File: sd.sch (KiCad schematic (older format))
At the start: 8 parts, among them J5 Micro_SD_Card_Det, U14 IP4220CZ6, U15 IP4220CZ6

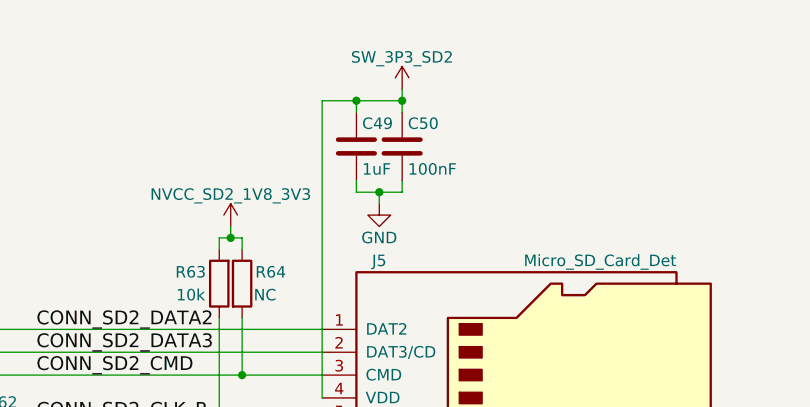
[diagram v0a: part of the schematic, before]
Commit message: Assign all associated signals to their respective pins on the EmCraft i.MX8M SoM
The ERC is now at the same state as the DART SoM schematic. Need to compare various aspects of the current schematic against the EmCraft reference design. The main buck-boost will likely need to be switched to a 5V regulator, or be configured to output 5V.

A regulator will likely need to be added which will output some VBAT voltage level (3.5~4.2V) for the M.2 cards. The SIM7100 for example requires at least 3.4V!
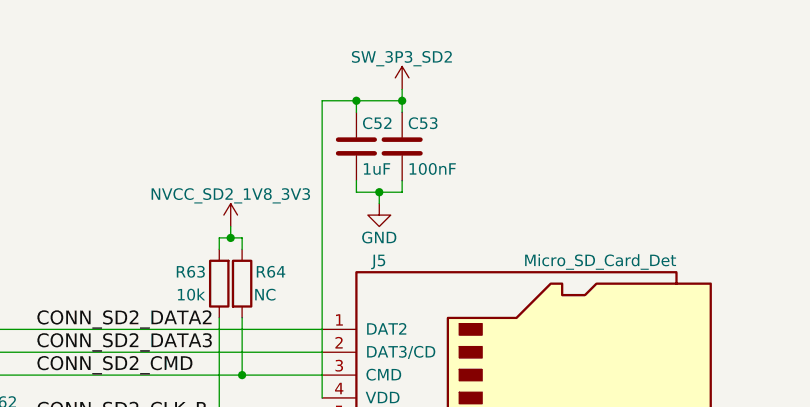
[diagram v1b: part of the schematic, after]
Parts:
- renumbered C49 to C52, C50 to C53
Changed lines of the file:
@@
 $EndComp
 $Comp
-L GND #PWR0119
+L GND #PWR0121
 U 1 1 5AC9FCAE
 P 5650 4550
-F 0 "#PWR0119" H 5650 4300 50  0001 C CNN
+F 0 "#PWR0121" H 5650 4300 50  0001 C CNN
 F 1 "GND" H 5650 4400 50  0000 C CNN
 F 2 "" H 5650 4550 50  0001 C CNN
@@
 $EndComp
 $Comp
-L GND #PWR0120
+L GND #PWR0122
 U 1 1 5ACA0128
 P 3850 4550
-F 0 "#PWR0120" H 3850 4300 50  0001 C CNN
+F 0 "#PWR0122" H 3850 4300 50  0001 C CNN
 F 1 "GND" H 3850 4400 50  0000 C CNN
 F 2 "" H 3850 4550 50  0001 C CNN
@@
 $EndComp
 $Comp
-L C C49
+L C C52
 U 1 1 5ACA0BD2
 P 4050 2800
-F 0 "C49" H 4075 2900 50  0000 L CNN
+F 0 "C52" H 4075 2900 50  0000 L CNN
 F 1 "1uF" H 4075 2700 50  0000 L CNN
 F 2 "" H 4088 2650 50  0001 C CNN
@@
 $EndComp
 $Comp
-L SW_3P3_SD2 #PWR0121
+L SW_3P3_SD2 #PWR0123
 U 1 1 5ACA0BF9
 P 4250 2550
-F 0 "#PWR0121" H 4250 2400 50  0001 C CNN
+F 0 "#PWR0123" H 4250 2400 50  0001 C CNN
 F 1 "SW_3P3_SD2" H 4250 2690 50  0000 C CNN
 F 2 "" H 4250 2550 50  0001 C CNN
@@
 $EndComp
 $Comp
-L NVCC_SD2_1V8_3V3 #PWR0122
+L NVCC_SD2_1V8_3V3 #PWR0124
 U 1 1 5ACA0C17
 P 3500 3150
-F 0 "#PWR0122" H 3500 3000 50  0001 C CNN
+F 0 "#PWR0124" H 3500 3000 50  0001 C CNN
 F 1 "NVCC_SD2_1V8_3V3" H 3500 3290 50  0000 C CNN
 F 2 "" H 3500 3150 50  0001 C CNN
@@
 $EndComp
 $Comp
-L C C50
+L C C53
 U 1 1 5ACA10D0
 P 4250 2800
-F 0 "C50" H 4275 2900 50  0000 L CNN
+F 0 "C53" H 4275 2900 50  0000 L CNN
 F 1 "100nF" H 4275 2700 50  0000 L CNN
 F 2 "" H 4288 2650 50  0001 C CNN
@@
 $EndComp
 $Comp
-L GND #PWR0123
+L GND #PWR0125
 U 1 1 5ACA12D0
 P 4150 3050
-F 0 "#PWR0123" H 4150 2800 50  0001 C CNN
+F 0 "#PWR0125" H 4150 2800 50  0001 C CNN
 F 1 "GND" H 4150 2900 50  0000 C CNN
 F 2 "" H 4150 3050 50  0001 C CNN
@@
 NoConn ~ 7200 3250
 $Comp
-L GND #PWR0124
+L GND #PWR0126
 U 1 1 5ACB9D67
 P 8400 4550
-F 0 "#PWR0124" H 8400 4300 50  0001 C CNN
+F 0 "#PWR0126" H 8400 4300 50  0001 C CNN
 F 1 "GND" H 8400 4400 50  0000 C CNN
 F 2 "" H 8400 4550 50  0001 C CNN
@@
 Connection ~ 8400 4200
 $Comp
-L NVCC_SD2_1V8_3V3 #PWR0125
+L NVCC_SD2_1V8_3V3 #PWR0127
 U 1 1 5ACB9F80
 P 7000 2550
-F 0 "#PWR0125" H 7000 2400 50  0001 C CNN
+F 0 "#PWR0127" H 7000 2400 50  0001 C CNN
 F 1 "NVCC_SD2_1V8_3V3" H 7000 2690 50  0000 C CNN
 F 2 "" H 7000 2550 50  0001 C CNN

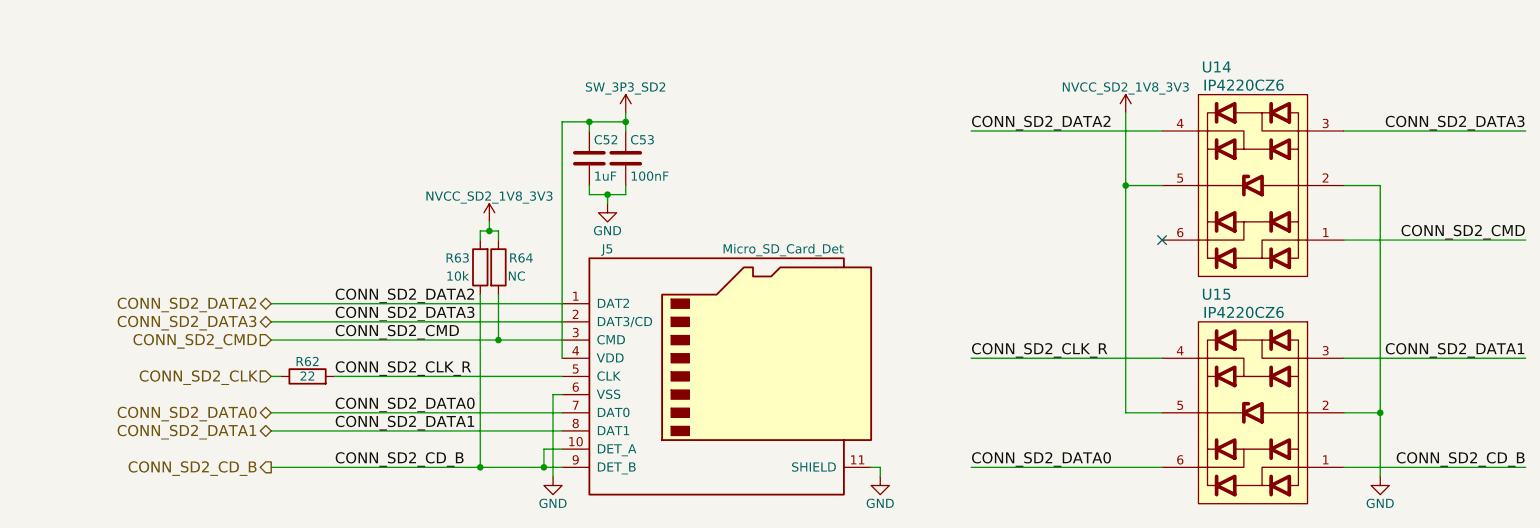
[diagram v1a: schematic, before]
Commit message: Use "Start to sheet number*100 and use first free number" designation, any new component added to the schematic will occupy the next available number in that sheet
For example: if sheet 2 has R201-R215 and we add a new resistor it will become R216.
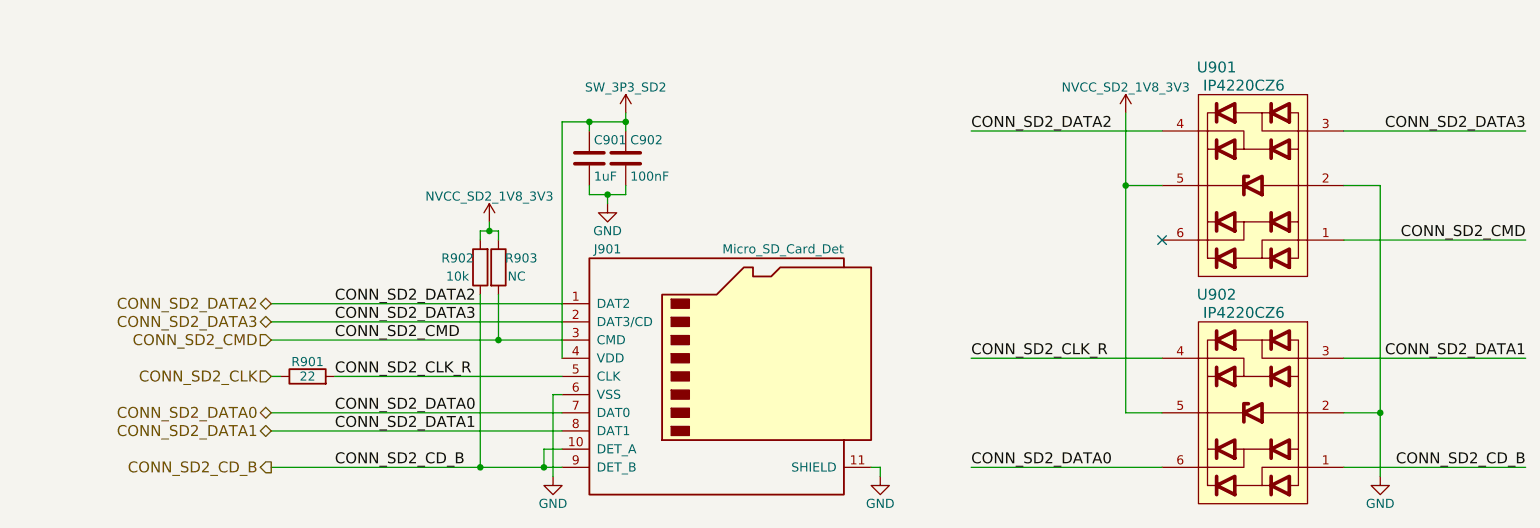
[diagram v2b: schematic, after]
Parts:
- renumbered C52 to C901, C53 to C902, J5 to J901, R62 to R901, R63 to R902, R64 to R903, U14 to U901, U15 to U902
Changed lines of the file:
@@
 $EndDescr
 $Comp
-L Micro_SD_Card_Det J5
+L Micro_SD_Card_Det J901
 U 1 1 5AC9C744
 P 4800 4000
-F 0 "J5" H 4150 4700 50  0000 C CNN
+F 0 "J901" H 4150 4700 50  0000 C CNN
 F 1 "Micro_SD_Card_Det" H 5450 4700 50  0000 R CNN
 F 2 "" H 6850 4700 50  0001 C CNN
@@
 CONN_SD2_CD_B
 $Comp
-L R R62
+L R R901
 U 1 1 5AC9FC3A
 P 2500 4000
-F 0 "R62" V 2580 4000 50  0000 C CNN
+F 0 "R901" V 2580 4000 50  0000 C CNN
 F 1 "22" V 2500 4000 50  0000 C CNN
 F 2 "" V 2430 4000 50  0001 C CNN
@@
 $EndComp
 $Comp
-L GND #PWR0121
+L GND #PWR905
 U 1 1 5AC9FCAE
 P 5650 4550
-F 0 "#PWR0121" H 5650 4300 50  0001 C CNN
+F 0 "#PWR905" H 5650 4300 50  0001 C CNN
 F 1 "GND" H 5650 4400 50  0000 C CNN
 F 2 "" H 5650 4550 50  0001 C CNN
@@
 $EndComp
 $Comp
-L GND #PWR0122
+L GND #PWR902
 U 1 1 5ACA0128
 P 3850 4550
-F 0 "#PWR0122" H 3850 4300 50  0001 C CNN
+F 0 "#PWR902" H 3850 4300 50  0001 C CNN
 F 1 "GND" H 3850 4400 50  0000 C CNN
 F 2 "" H 3850 4550 50  0001 C CNN
@@
 $EndComp
 $Comp
-L R R63
+L R R902
 U 1 1 5ACA0594
 P 3450 3400
-F 0 "R63" H 3575 3350 50  0000 C CNN
+F 0 "R902" H 3575 3350 50  0000 C CNN
 F 1 "10k" H 3575 3450 50  0000 C CNN
 F 2 "" V 3380 3400 50  0001 C CNN
@@
 $EndComp
 $Comp
-L R R64
+L R R903
 U 1 1 5ACA05C1
 P 3550 3400
-F 0 "R64" H 3675 3450 50  0000 C CNN
+F 0 "R903" H 3675 3450 50  0000 C CNN
 F 1 "NC" H 3650 3350 50  0000 C CNN
 F 2 "" V 3480 3400 50  0001 C CNN
@@
 $EndComp
 $Comp
-L C C52
+L C C901
 U 1 1 5ACA0BD2
 P 4050 2800
-F 0 "C52" H 4075 2900 50  0000 L CNN
+F 0 "C901" H 4075 2900 50  0000 L CNN
 F 1 "1uF" H 4075 2700 50  0000 L CNN
 F 2 "" H 4088 2650 50  0001 C CNN
@@
 $EndComp
 $Comp
-L SW_3P3_SD2 #PWR0123
+L SW_3P3_SD2 #PWR904
 U 1 1 5ACA0BF9
 P 4250 2550
-F 0 "#PWR0123" H 4250 2400 50  0001 C CNN
+F 0 "#PWR904" H 4250 2400 50  0001 C CNN
 F 1 "SW_3P3_SD2" H 4250 2690 50  0000 C CNN
 F 2 "" H 4250 2550 50  0001 C CNN
@@
 $EndComp
 $Comp
-L NVCC_SD2_1V8_3V3 #PWR0124
+L NVCC_SD2_1V8_3V3 #PWR901
 U 1 1 5ACA0C17
 P 3500 3150
-F 0 "#PWR0124" H 3500 3000 50  0001 C CNN
+F 0 "#PWR901" H 3500 3000 50  0001 C CNN
 F 1 "NVCC_SD2_1V8_3V3" H 3500 3290 50  0000 C CNN
 F 2 "" H 3500 3150 50  0001 C CNN
@@
 $EndComp
 $Comp
-L C C53
+L C C902
 U 1 1 5ACA10D0
 P 4250 2800
-F 0 "C53" H 4275 2900 50  0000 L CNN
+F 0 "C902" H 4275 2900 50  0000 L CNN
 F 1 "100nF" H 4275 2700 50  0000 L CNN
 F 2 "" H 4288 2650 50  0001 C CNN
@@
 $EndComp
 $Comp
-L GND #PWR0125
+L GND #PWR903
 U 1 1 5ACA12D0
 P 4150 3050
-F 0 "#PWR0125" H 4150 2800 50  0001 C CNN
+F 0 "#PWR903" H 4150 2800 50  0001 C CNN
 F 1 "GND" H 4150 2900 50  0000 C CNN
 F 2 "" H 4150 3050 50  0001 C CNN
@@
 Connection ~ 3550 3800
 $Comp
-L IP4220CZ6 U14
+L IP4220CZ6 U901
 U 1 1 5ACB95D7
 P 7700 2950
-F 0 "U14" H 7500 3600 60  0000 C CNN
+F 0 "U901" H 7500 3600 60  0000 C CNN
 F 1 "IP4220CZ6" H 7650 3500 60  0000 C CNN
 F 2 "" V 7675 2950 60  0001 C CNN
@@
 $EndComp
 $Comp
-L IP4220CZ6 U15
+L IP4220CZ6 U902
 U 1 1 5ACB960B
 P 7700 4200
-F 0 "U15" H 7500 4850 60  0000 C CNN
+F 0 "U902" H 7500 4850 60  0000 C CNN
 F 1 "IP4220CZ6" H 7650 4750 60  0000 C CNN
 F 2 "" V 7675 4200 60  0001 C CNN
@@
 NoConn ~ 7200 3250
 $Comp
-L GND #PWR0126
+L GND #PWR907
 U 1 1 5ACB9D67
 P 8400 4550
-F 0 "#PWR0126" H 8400 4300 50  0001 C CNN
+F 0 "#PWR907" H 8400 4300 50  0001 C CNN
 F 1 "GND" H 8400 4400 50  0000 C CNN
 F 2 "" H 8400 4550 50  0001 C CNN
@@
 Connection ~ 8400 4200
 $Comp
-L NVCC_SD2_1V8_3V3 #PWR0127
+L NVCC_SD2_1V8_3V3 #PWR906
 U 1 1 5ACB9F80
 P 7000 2550
-F 0 "#PWR0127" H 7000 2400 50  0001 C CNN
+F 0 "#PWR906" H 7000 2400 50  0001 C CNN
 F 1 "NVCC_SD2_1V8_3V3" H 7000 2690 50  0000 C CNN
 F 2 "" H 7000 2550 50  0001 C CNN

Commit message: Move reference designators in the schematic so that they are legible
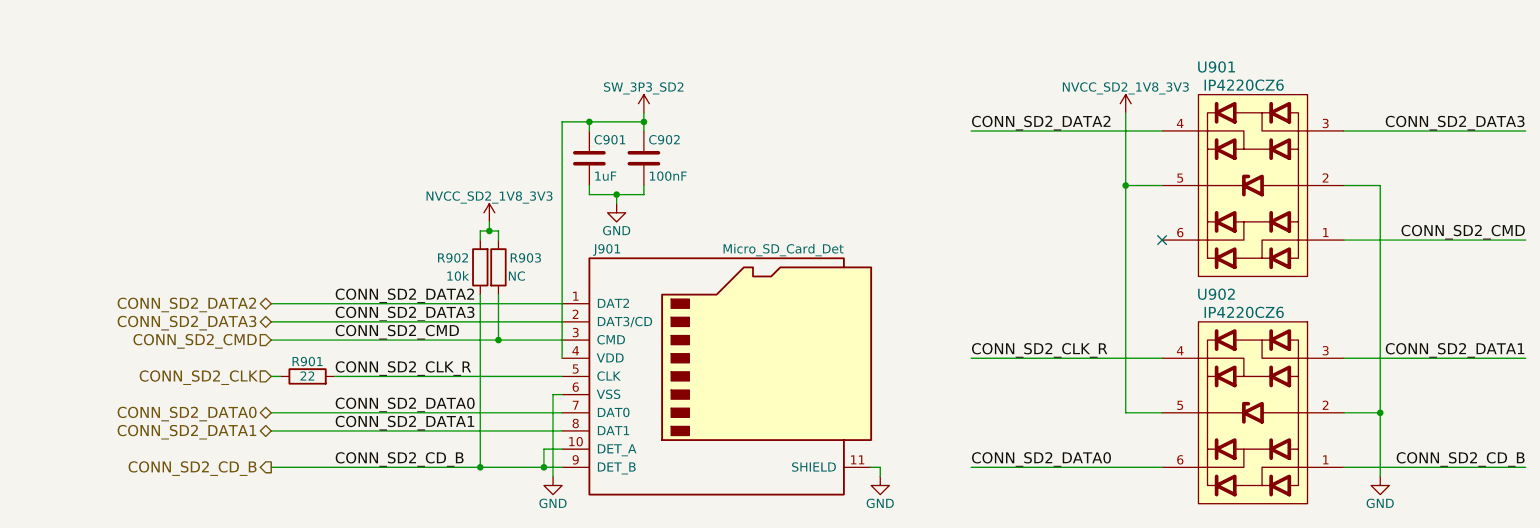
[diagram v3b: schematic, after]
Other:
- moved on the sheet: C902
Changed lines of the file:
@@
 $EndComp
 $Comp
-L GND #PWR905
+L GND #PWR0121
 U 1 1 5AC9FCAE
 P 5650 4550
-F 0 "#PWR905" H 5650 4300 50  0001 C CNN
+F 0 "#PWR0121" H 5650 4300 50  0001 C CNN
 F 1 "GND" H 5650 4400 50  0000 C CNN
 F 2 "" H 5650 4550 50  0001 C CNN
@@
 $EndComp
 $Comp
-L GND #PWR902
+L GND #PWR0122
 U 1 1 5ACA0128
 P 3850 4550
-F 0 "#PWR902" H 3850 4300 50  0001 C CNN
+F 0 "#PWR0122" H 3850 4300 50  0001 C CNN
 F 1 "GND" H 3850 4400 50  0000 C CNN
 F 2 "" H 3850 4550 50  0001 C CNN
@@
 U 1 1 5ACA0594
 P 3450 3400
-F 0 "R902" H 3575 3350 50  0000 C CNN
+F 0 "R902" H 3600 3350 50  0000 C CNN
 F 1 "10k" H 3575 3450 50  0000 C CNN
 F 2 "" V 3380 3400 50  0001 C CNN
@@
 U 1 1 5ACA05C1
 P 3550 3400
-F 0 "R903" H 3675 3450 50  0000 C CNN
+F 0 "R903" H 3700 3450 50  0000 C CNN
 F 1 "NC" H 3650 3350 50  0000 C CNN
 F 2 "" V 3480 3400 50  0001 C CNN
@@
 $EndComp
 $Comp
-L SW_3P3_SD2 #PWR904
+L SW_3P3_SD2 #PWR0123
 U 1 1 5ACA0BF9
-P 4250 2550
-F 0 "#PWR904" H 4250 2400 50  0001 C CNN
-F 1 "SW_3P3_SD2" H 4250 2690 50  0000 C CNN
-F 2 "" H 4250 2550 50  0001 C CNN
-F 3 "" H 4250 2550 50  0001 C CNN
-	1    4250 2550
-	1    0    0    -1
-$EndComp
-$Comp
-L NVCC_SD2_1V8_3V3 #PWR901
+P 4350 2550
+F 0 "#PWR0123" H 4350 2400 50  0001 C CNN
+F 1 "SW_3P3_SD2" H 4350 2690 50  0000 C CNN
+F 2 "" H 4350 2550 50  0001 C CNN
+F 3 "" H 4350 2550 50  0001 C CNN
+	1    4350 2550
+	1    0    0    -1
+$EndComp
+$Comp
+L NVCC_SD2_1V8_3V3 #PWR0124
 U 1 1 5ACA0C17
 P 3500 3150
-F 0 "#PWR901" H 3500 3000 50  0001 C CNN
+F 0 "#PWR0124" H 3500 3000 50  0001 C CNN
 F 1 "NVCC_SD2_1V8_3V3" H 3500 3290 50  0000 C CNN
 F 2 "" H 3500 3150 50  0001 C CNN
@@
 L C C902
 U 1 1 5ACA10D0
-P 4250 2800
-F 0 "C902" H 4275 2900 50  0000 L CNN
-F 1 "100nF" H 4275 2700 50  0000 L CNN
-F 2 "" H 4288 2650 50  0001 C CNN
-F 3 "" H 4250 2800 50  0001 C CNN
-	1    4250 2800
-	1    0    0    -1
-$EndComp
-$Comp
-L GND #PWR903
+P 4350 2800
+F 0 "C902" H 4375 2900 50  0000 L CNN
+F 1 "100nF" H 4375 2700 50  0000 L CNN
+F 2 "" H 4388 2650 50  0001 C CNN
+F 3 "" H 4350 2800 50  0001 C CNN
+	1    4350 2800
+	1    0    0    -1
+$EndComp
+$Comp
+L GND #PWR0125
 U 1 1 5ACA12D0
-P 4150 3050
-F 0 "#PWR903" H 4150 2800 50  0001 C CNN
-F 1 "GND" H 4150 2900 50  0000 C CNN
-F 2 "" H 4150 3050 50  0001 C CNN
-F 3 "" H 4150 3050 50  0001 C CNN
-	1    4150 3050
+P 4200 3050
+F 0 "#PWR0125" H 4200 2800 50  0001 C CNN
+F 1 "GND" H 4200 2900 50  0000 C CNN
+F 2 "" H 4200 3050 50  0001 C CNN
+F 3 "" H 4200 3050 50  0001 C CNN
+	1    4200 3050
 	1    0    0    -1
 $EndComp
@@
 	2300 3700 3900 3700
 Wire Wire Line
-	2300 3800 3900 3800
+	2300 3800 3550 3800
+Wire Wire Line
+	3550 3800 3900 3800
 Wire Wire Line
 	2300 4200 3900 4200
@@
 	2300 4300 3900 4300
 Wire Wire Line
-	2300 4500 3900 4500
+	2300 4500 3450 4500
+Wire Wire Line
+	3450 4500 3800 4500
+Wire Wire Line
+	3800 4500 3900 4500
 Wire Wire Line
 	3900 4400 3800 4400
@@
 	3550 3200 3550 3250
 Wire Wire Line
-	3450 3200 3550 3200
+	3450 3200 3500 3200
+Wire Wire Line
+	3500 3200 3550 3200
 Wire Wire Line
 	3500 3150 3500 3200
@@
 	3900 3900 3900 2600
 Wire Wire Line
-	3900 2600 4250 2600
-Wire Wire Line
-	4250 2550 4250 2650
+	3900 2600 4050 2600
+Wire Wire Line
+	4050 2600 4350 2600
+Wire Wire Line
+	4350 2550 4350 2600
+Wire Wire Line
+	4350 2600 4350 2650
 Wire Wire Line
 	4050 2650 4050 2600
@@
 	4050 2950 4050 3000
 Wire Wire Line
-	4050 3000 4250 3000
-Wire Wire Line
-	4250 3000 4250 2950
-Wire Wire Line
-	4150 3050 4150 3000
-Connection ~ 4150 3000
-Connection ~ 4250 2600
+	4050 3000 4200 3000
+Wire Wire Line
+	4200 3000 4350 3000
+Wire Wire Line
+	4350 3000 4350 2950
+Wire Wire Line
+	4200 3050 4200 3000
+Connection ~ 4200 3000
+Connection ~ 4350 2600
 Wire Wire Line
 	3450 3550 3450 4500
@@
 NoConn ~ 7200 3250
 $Comp
-L GND #PWR907
+L GND #PWR0126
 U 1 1 5ACB9D67
 P 8400 4550
-F 0 "#PWR907" H 8400 4300 50  0001 C CNN
+F 0 "#PWR0126" H 8400 4300 50  0001 C CNN
 F 1 "GND" H 8400 4400 50  0000 C CNN
 F 2 "" H 8400 4550 50  0001 C CNN
@@
 $EndComp
 Wire Wire Line
-	8400 2950 8400 4550
+	8400 2950 8400 4200
+Wire Wire Line
+	8400 4200 8400 4550
 Wire Wire Line
 	8400 4200 8200 4200
@@
 Connection ~ 8400 4200
 $Comp
-L NVCC_SD2_1V8_3V3 #PWR906
+L NVCC_SD2_1V8_3V3 #PWR0127
 U 1 1 5ACB9F80
 P 7000 2550
-F 0 "#PWR906" H 7000 2400 50  0001 C CNN
+F 0 "#PWR0127" H 7000 2400 50  0001 C CNN
 F 1 "NVCC_SD2_1V8_3V3" H 7000 2690 50  0000 C CNN
 F 2 "" H 7000 2550 50  0001 C CNN
@@
 $EndComp
 Wire Wire Line
-	7000 2550 7000 4200
+	7000 2550 7000 2950
+Wire Wire Line
+	7000 2950 7000 4200
 Wire Wire Line
 	7000 4200 7200 4200
